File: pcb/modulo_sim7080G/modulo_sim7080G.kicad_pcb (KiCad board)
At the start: 2 copper layers, 70 x 70 mm, 9 parts, among them J1 Conn_01x02, J2 Conn_01x02, J3 Conn_01x07, U1 SIM7080G, U2 TXB0108DQSR

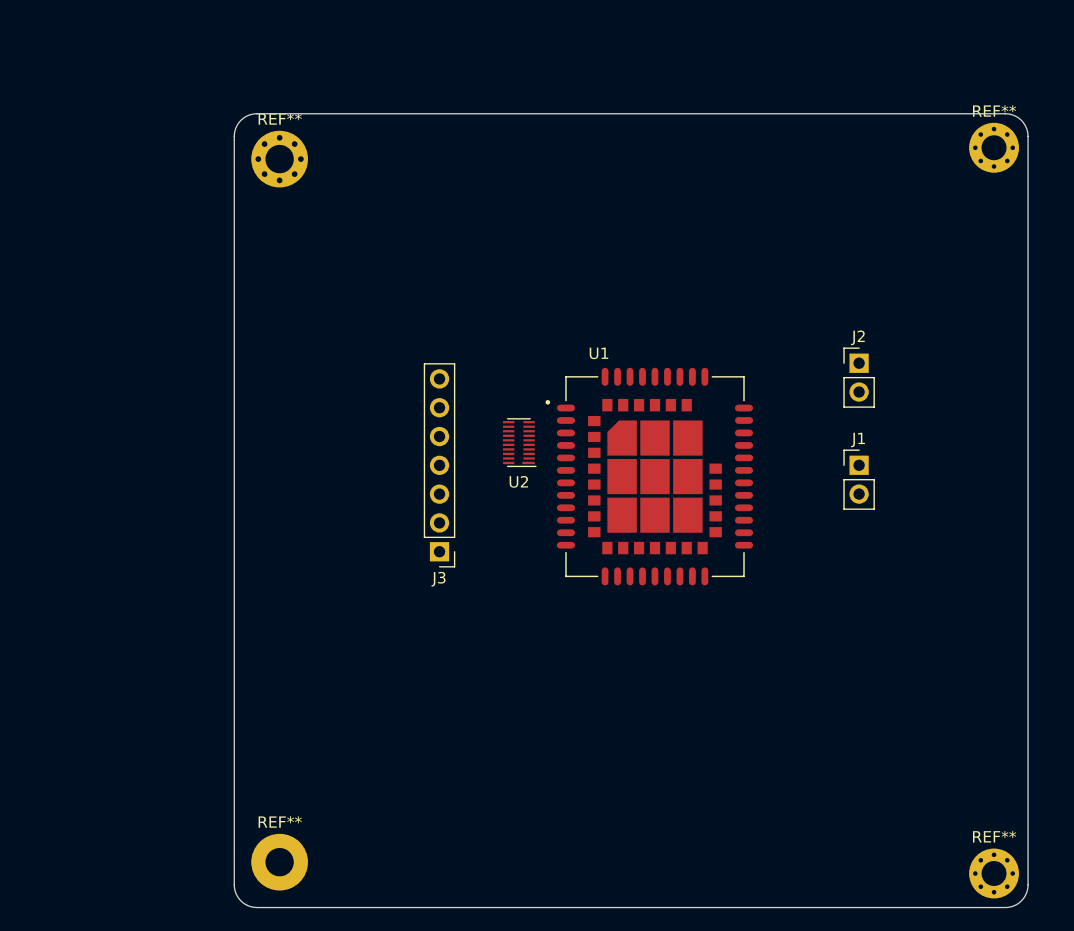
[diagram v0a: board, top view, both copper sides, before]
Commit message: update schematic
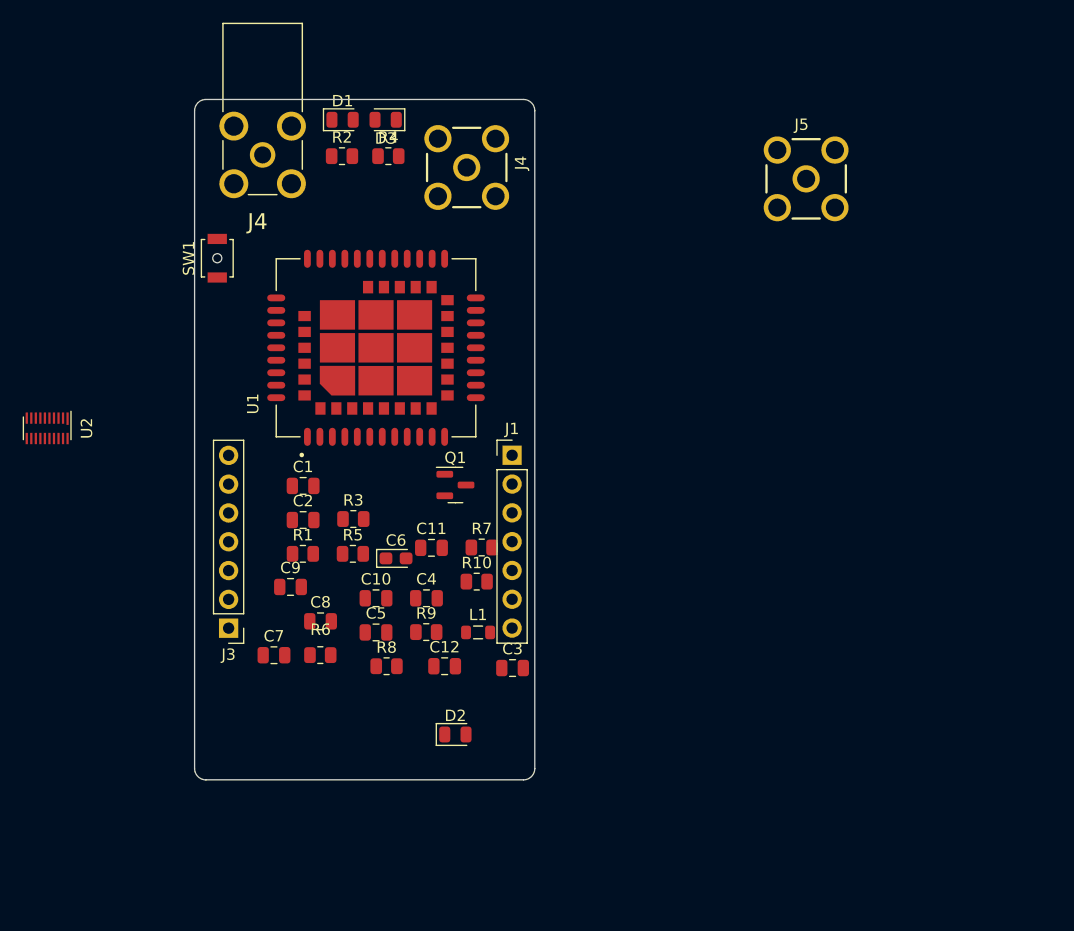
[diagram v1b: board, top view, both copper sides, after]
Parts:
- removed J2: Conn_01x02, Connector_PinHeader_2.54mm:PinHeader_1x02_P2.54mm_Vertical
- removed REF**: MountingHole_2.5mm_Pad, MountingHole:MountingHole_2.5mm_Pad
- removed REF** (x2): MountingHole_2.2mm_M2_Pad_Via, MountingHole:MountingHole_2.2mm_M2_Pad_Via
- removed REF**: MountingHole_2.5mm_Pad_Via, MountingHole:MountingHole_2.5mm_Pad_Via
- added C1: C_Small, Capacitor_SMD:C_0805_2012Metric, F.Cu at (105.1, 98.8)
- added C10: 100nf, Capacitor_SMD:C_0805_2012Metric, F.Cu at (111.5, 108.7)
- added C11: 100pf, Capacitor_SMD:C_0805_2012Metric, F.Cu at (116.4, 104.3)
- added C12: 100pf, Capacitor_SMD:C_0805_2012Metric, F.Cu at (117.5, 114.7)
- added C2: C_Small, Capacitor_SMD:C_0805_2012Metric, F.Cu at (105.1, 101.8)
- added C3: 10pf, Capacitor_SMD:C_0805_2012Metric, F.Cu at (123.5, 114.9)
- added C4: 33pf, Capacitor_SMD:C_0805_2012Metric, F.Cu at (116.0, 108.7)
- added C5: 100nf, Capacitor_SMD:C_0805_2012Metric, F.Cu at (111.5, 111.7)
- added C6: 470uf, Capacitor_Tantalum_SMD:CP_EIA-2012-12_Kemet-R, F.Cu at (113.3, 105.2)
- added C7: 100pf, Capacitor_SMD:C_0805_2012Metric, F.Cu at (102.5, 113.8)
- added C8: 100pf, Capacitor_SMD:C_0805_2012Metric, F.Cu at (106.6, 110.8)
- added C9: 100pf, Capacitor_SMD:C_0805_2012Metric, F.Cu at (104.0, 107.7)
- added D1: LED, LED_SMD:LED_0805_2012Metric, F.Cu at (108.5, 66.5)
- added D2: LED, LED_SMD:LED_0805_2012Metric, F.Cu at (118.5, 120.7)
- added D3: LED, LED_SMD:LED_0805_2012Metric, F.Cu at (112.3, 66.5)
- added J4: SMA-J-P-X-RA-TH1, SMA-J-P-X-RA-TH1:SAMTEC_SMA-J-P-X-RA-TH1, F.Cu at (119.5, 70.7)
- added J4: 901-143-6RFX, 901-143-6RFX:AMPHENOL_901-143-6RFX, F.Cu at (101.5, 69.6)
- added J5: SMA-J-P-X-RA-TH1, SMA-J-P-X-RA-TH1:SAMTEC_SMA-J-P-X-RA-TH1, F.Cu at (149.4, 71.7)
- added L1: 47nH, Inductor_SMD:L_0805_2012Metric, F.Cu at (120.5, 111.7)
- added Q1: BC846, Package_TO_SOT_SMD:SOT-23, F.Cu at (118.5, 98.7)
- added R1: R_Small, Resistor_SMD:R_0805_2012Metric, F.Cu at (105.0, 104.8)
- added R10: 0, Resistor_SMD:R_0805_2012Metric, F.Cu at (120.4, 107.3)
- added R2: R_Small, Resistor_SMD:R_0805_2012Metric, F.Cu at (108.5, 69.7)
- added R3: R_Small, Resistor_SMD:R_0805_2012Metric, F.Cu at (109.5, 101.7)
- added R4: R_Small, Resistor_SMD:R_0805_2012Metric, F.Cu at (112.6, 69.7)
- added R5: R_Small, Resistor_SMD:R_0805_2012Metric, F.Cu at (109.5, 104.8)
- added R6: 4.7K, Resistor_SMD:R_0805_2012Metric, F.Cu at (106.6, 113.7)
- added R7: 47K, Resistor_SMD:R_0805_2012Metric, F.Cu at (120.8, 104.2)
- added R8: 10, Resistor_SMD:R_0805_2012Metric, F.Cu at (112.4, 114.7)
- added R9: 0, Resistor_SMD:R_0805_2012Metric, F.Cu at (115.9, 111.7)
- added SW1: SW_Push, Button_Switch_SMD:SW_SPST_B3U-1000P-B, F.Cu at (97.5, 78.7)
- J1: value Conn_01x02 -> Conn_01x07; footprint Connector_PinHeader_2.54mm:PinHeader_1x02_P2.54mm_Vertical -> Connector_PinHeader_2.54mm:PinHeader_1x07_P2.54mm_Vertical
- moved U2 41.6 mm to (82.5, 93.7), turned to -90 degrees
- moved J1 30.6 mm to (123.5, 96.1)
- moved U1 27.1 mm to (111.5, 86.6), turned to 90 degrees
- moved J3 19.8 mm to (98.5, 111.4)
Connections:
- net Net-(U1-Pad22) renamed /UART2_TXD
- net Net-(U1-Pad23) renamed /UART2_RXD
- U1 pad 32: unconnected-(U1-Pad32) -> Net-(U1-Pad32)
- U1 pad 34: Net-(U1-Pad34) -> +3.3V
- U1 pad 35: Net-(U1-Pad34) -> +3.3V
- U1 pad 39: unconnected-(U1-Pad39) -> /PWRKEY
- U1 pad 61: Net-(U1-Pad61) -> /UART3_TXD
- U1 pad 62: Net-(U1-Pad62) -> /UART3_RXD
- U1 pad 68: unconnected-(U1-Pad68) -> /GNSS_ANT
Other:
- board size 70 x 70 mm -> 30 x 60 mm

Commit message: antes del gitignore
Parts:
- removed the J4 at (119.5, 70.7)
- removed the J4 at (101.5, 69.6)
- added C13: 0.1uf, Capacitor_SMD:C_0402_1005Metric, F.Cu at (164.9, 83.3)
- added C14: 0.1uf, Capacitor_SMD:C_0402_1005Metric, F.Cu at (164.9, 86.3)
- added C15: 33pf, Capacitor_SMD:C_0402_1005Metric, F.Cu at (111.5, 99.8)
- added C16: 100nf, Capacitor_SMD:C_0402_1005Metric, F.Cu at (111.5, 97.8)
- added F1: Fuse_Small, Fuse:Fuse_0402_1005Metric, F.Cu at (109.0, 107.7)
- added J2: Conn_01x07, Connector_PinHeader_2.54mm:PinHeader_1x07_P2.54mm_Vertical, F.Cu at (122.5, 95.2)
- added J4: SMA-J-P-X-RA-TH1, SMA-J-P-X-RA-TH1:SAMTEC_SMA-J-P-X-RA-TH1, F.Cu at (120.0, 69.7)
- added R11: 10k, Resistor_SMD:R_0402_1005Metric, F.Cu at (169.3, 83.3)
- added R12: 10k, Resistor_SMD:R_0402_1005Metric, F.Cu at (169.3, 86.2)
- added R13: 2.2k, Resistor_SMD:R_0402_1005Metric, F.Cu at (101.7, 107.7)
- added U3: TXB0108PWR, footprints:PW0020A_N, F.Cu at (105.0, 101.7)
- added U4: PDTC114EU, footprints2:SOT323_NEX, F.Cu at (112.5, 71.6)
- C1, C2: value C_Small -> 33pf; footprint Capacitor_SMD:C_0805_2012Metric -> Capacitor_SMD:C_0402_1005Metric
- C10, C11, C12, C4, C5, C7, C8, C9: footprint Capacitor_SMD:C_0805_2012Metric -> Capacitor_SMD:C_0402_1005Metric
- J3: value Conn_01x07 -> SMA-J-P-X-RA-TH1; footprint Connector_PinHeader_2.54mm:PinHeader_1x07_P2.54mm_Vertical -> SMA-J-P-X-RA-TH1:SAMTEC_SMA-J-P-X-RA-TH1
- J5: value SMA-J-P-X-RA-TH1 -> USB_B_Micro; footprint SMA-J-P-X-RA-TH1:SAMTEC_SMA-J-P-X-RA-TH1 -> Connector_USB:USB_Micro-B_Molex_47346-0001
- R1: value R_Small -> 1M; footprint Resistor_SMD:R_0805_2012Metric -> Resistor_SMD:R_0402_1005Metric
- R10, R3, R4, R5, R6, R7, R8, R9: footprint Resistor_SMD:R_0805_2012Metric -> Resistor_SMD:R_0402_1005Metric
- R2: value R_Small -> 1K; footprint Resistor_SMD:R_0805_2012Metric -> Resistor_SMD:R_0402_1005Metric
- U2: value TXB0108DQSR -> PDTC114EU; footprint Package_SON:USON-20_2x4mm_P0.4mm -> footprints2:SOT323_NEX
- moved J5 59.0 mm to (105.5, 111.1)
- moved D2 54.2 mm to (107.5, 67.7), turned to -90 degrees
- moved C5 52.2 mm to (153.8, 81.2)
- moved R6 50.6 mm to (144.5, 80.2)
- moved C3 49.9 mm to (153.8, 75.2)
- moved C4 48.6 mm to (153.8, 78.2)
- moved R4 46.7 mm to (137.5, 109.2)
- moved L1 42.4 mm to (99.0, 75.2)
- moved J3 41.8 mm to (101.0, 69.7), turned to -90 degrees
- moved SW1 40.0 mm to (136.9, 71.8)
- moved Q1 38.5 mm to (145.4, 71.3)
- moved R2 38.3 mm to (104.0, 107.7)
- moved D1 36.7 mm to (145.2, 65.2)
- moved U2 33.8 mm to (108.0, 71.6), turned to 0 degrees
- moved R7 31.7 mm to (144.5, 83.2)
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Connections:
- net /UART2_RXD renamed /modulo_celular/UART2_RXD
- net /UART2_TXD renamed /modulo_celular/UART2_TXD
- net /UART3_RXD renamed /modulo_celular/UART3_RXD
- net /UART3_TXD renamed /modulo_celular/UART3_TXD
- C1 pad 1: VDD -> Net-(J6-RST)
- C11 pad 1: Net-(U1-Pad32) -> Net-(C11-Pad1)
- C2 pad 1: +3.3V -> Net-(J6-CLK)
- C8 pad 2: Net-(J5-Pad1) -> Net-(C8-Pad2)
- C9 pad 1: Net-(J5-Pad1) -> Net-(C8-Pad2)
- D2 pad 1: GND -> Net-(D2-K)
- D3 pad 1: GND -> Net-(D3-K)
- J1 pad 6: /PIN_PWRKEY -> /modulo_celular/PIN_PWRKEY
- J3 pad 1: Net-(J3-Pad1) -> Net-(C8-Pad2)
- J3 pad 2: Net-(J3-Pad2) -> GND
- J3 pad 3: Net-(J3-Pad3) -> GND
- J3 pad 4: Net-(J3-Pad4) -> GND
- J3 pad 5: Net-(J3-Pad5) -> GND
- J5 pad 1: Net-(J5-Pad1) -> Net-(J5-VBUS)
- J5 pad 2: GND -> Net-(J5-D-)
- J5 pad 3: GND -> Net-(J5-D+)
- J5 pad 4: GND -> Net-(J5-ID)
- L1 pad 2: Net-(J5-Pad1) -> Net-(C8-Pad2)
- Q1 pad 3: /PWRKEY -> /signals_input_output/PWRKEY
- R1 pad 1: Net-(R1-Pad1) -> Net-(J5-ID)
- R2 pad 1: GND -> Net-(U1-USB_VBUS)
- R2 pad 2: Net-(R2-Pad2) -> Net-(F1-Pad2)
- R4 pad 1: /LED_STATUS -> +3.3V
- R5 pad 1: /LED_NETLIGHT -> +3.3V
- R6 pad 2: /PIN_PWRKEY -> /signals_input_output/PIN_PWRKEY
- R9 pad 1: Net-(U1-Pad32) -> Net-(C11-Pad1)
- SW1 pad 1: /PWRKEY -> /signals_input_output/PWRKEY
- U1 pad 1: /UART1_TXD -> /modulo_celular/UART1_TXD
- U1 pad 15: unconnected-(U1-Pad15) -> /modulo_celular/I/O
- U1 pad 16: unconnected-(U1-Pad16) -> Net-(J6-CLK)
- U1 pad 17: unconnected-(U1-Pad17) -> Net-(J6-RST)
- U1 pad 18: unconnected-(U1-Pad18) -> Net-(J6-VCC)
- U1 pad 2: /UART1_RXD -> /modulo_celular/UART1_RXD
- U1 pad 24: unconnected-(U1-Pad24) -> Net-(U1-USB_VBUS)
- U1 pad 25: unconnected-(U1-Pad25) -> Net-(J5-D+)
- U1 pad 26: unconnected-(U1-Pad26) -> Net-(J5-D-)
- U1 pad 3: /UART1_RTS -> /modulo_celular/UART1_RTS
- U1 pad 32: Net-(U1-Pad32) -> /modulo_celular/RF_ANT
- U1 pad 39: /PWRKEY -> /modulo_celular/PWRKEY
- U1 pad 4: /UART1_CTS -> /modulo_celular/UART1_CTS
- U1 pad 41: /LED_NETLIGHT -> /modulo_celular/LED_NETLIGHT
- U1 pad 42: /LED_STATUS -> /modulo_celular/LED_STATUS
- U1 pad 5: /UART1_DCD -> /modulo_celular/UART1_DCD
- U1 pad 6: /UART1_DTR -> /modulo_celular/UART1_DTR
- U1 pad 68: /GNSS_ANT -> /modulo_celular/GNSS_ANT
- U1 pad 7: /UART1_RI -> /modulo_celular/UART1_RI
- U2 pad 1: /UART1_CTS -> /signals_input_output/LED_STATUS
- U2 pad 2: /UART1_DCD -> GND
- U2 pad 3: /UART1_DTR -> Net-(D2-K)
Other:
- board size 30 x 60 mm -> 30 x 50 mm

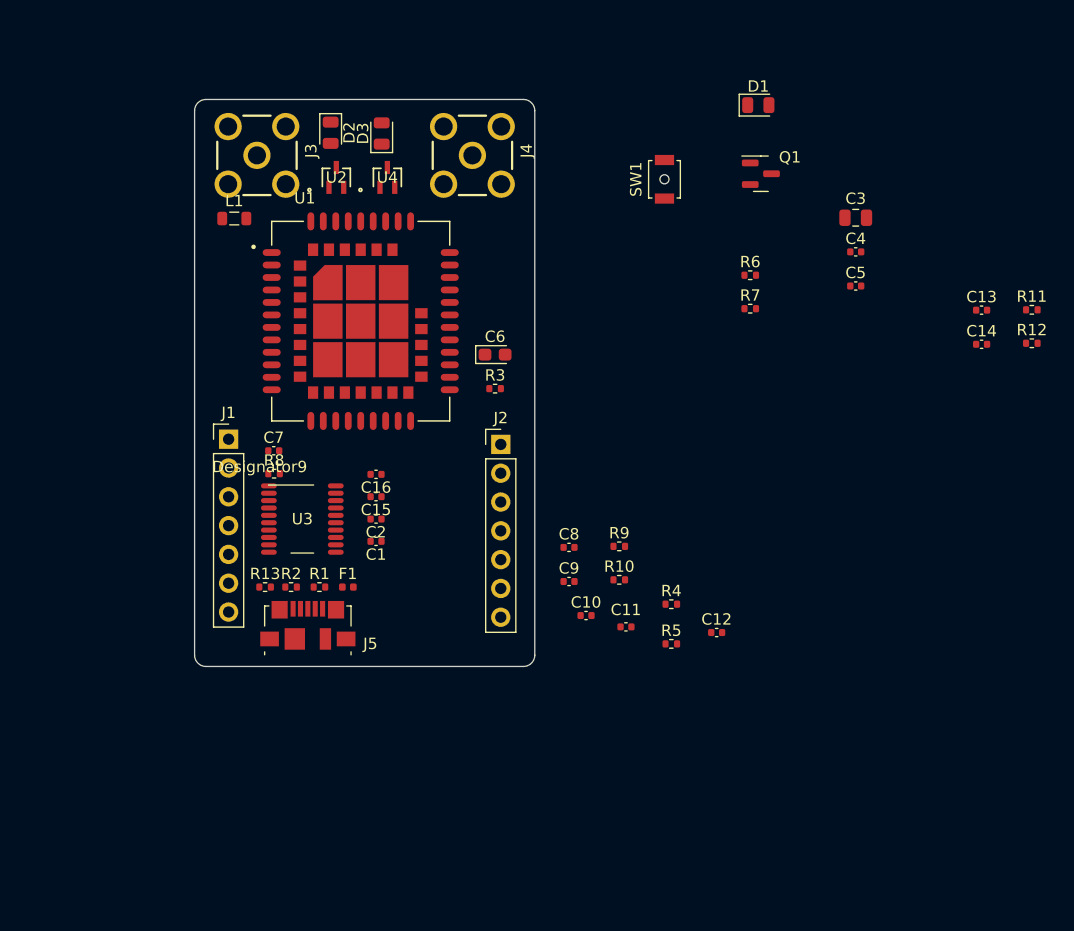
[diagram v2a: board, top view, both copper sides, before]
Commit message: se ordenaron los componentes en el pcb
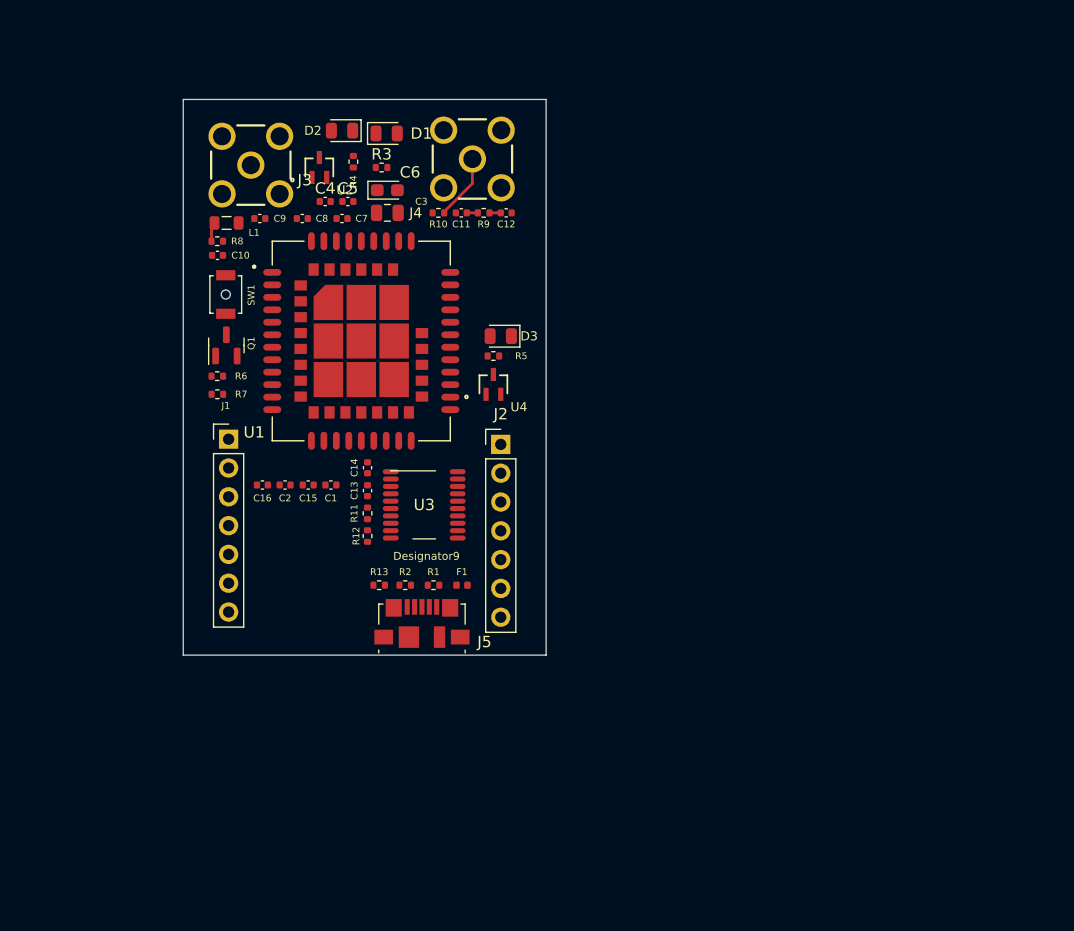
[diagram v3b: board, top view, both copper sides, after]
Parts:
- moved R11 61.3 mm to (110.8, 101.2), turned to 90 degrees
- moved R12 61.0 mm to (110.8, 103.2), turned to -90 degrees
- moved C13 56.4 mm to (110.8, 99.2), turned to 90 degrees
- moved C14 55.2 mm to (110.8, 97.2), turned to 90 degrees
- moved Q1 49.5 mm to (98.3, 86.4), turned to 90 degrees
- moved R4 48.0 mm to (109.5, 70.2), turned to -90 degrees
- moved R6 47.8 mm to (97.5, 89.1)
- moved R7 47.6 mm to (97.5, 90.7)
- moved C4 47.0 mm to (107.0, 73.7)
- moved C10 45.4 mm to (97.5, 78.5)
- moved C5 45.4 mm to (109.0, 73.7)
- moved C9 42.1 mm to (101.2, 75.2)
- moved C12 41.4 mm to (123.0, 74.7)
- moved C3 41.3 mm to (112.5, 74.7), turned to 180 degrees
- moved SW1 40.0 mm to (98.2, 81.9), turned to -90 degrees
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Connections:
- net /modulo_celular/GNSS_ANT renamed /antenas/GNSS_ANT
- C11 pad 1: Net-(C11-Pad1) -> /antenas/RF_ANT
- Q1 pad 3: /signals_input_output/PWRKEY -> /modulo_celular/PWRKEY
- R6 pad 2: /signals_input_output/PIN_PWRKEY -> /modulo_celular/PIN_PWRKEY
- R9 pad 1: Net-(C11-Pad1) -> /antenas/RF_ANT
- SW1 pad 1: /signals_input_output/PWRKEY -> /modulo_celular/PWRKEY
- U1 pad 1: /modulo_celular/UART1_TXD -> /level_shifters/UART1_TXD
- U1 pad 2: /modulo_celular/UART1_RXD -> /level_shifters/UART1_RXD
- U1 pad 3: /modulo_celular/UART1_RTS -> /level_shifters/UART1_RTS
- U1 pad 32: /modulo_celular/RF_ANT -> /antenas/RF_ANT
- U1 pad 4: /modulo_celular/UART1_CTS -> /level_shifters/UART1_CTS
- U1 pad 5: /modulo_celular/UART1_DCD -> /level_shifters/UART1_DCD
- U1 pad 6: /modulo_celular/UART1_DTR -> /level_shifters/UART1_DTR
- U1 pad 7: /modulo_celular/UART1_RI -> /level_shifters/UART1_RI
- U2 pad 1: /signals_input_output/LED_STATUS -> /modulo_celular/LED_NETLIGHT
- U4 pad 1: /signals_input_output/LED_NETLIGHT -> /modulo_celular/LED_STATUS
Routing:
- net Net-(J4-Pad1): track 0.00 -> 5.78 mm
- net Net-(L1-Pad1): track 0.00 -> 1.61 mm
- net Net-(C12-Pad1): track 0.00 -> 1.00 mm
- net /antenas/RF_ANT: track 0.00 -> 0.98 mm
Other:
- board size 30 x 50 mm -> 32 x 49 mm
